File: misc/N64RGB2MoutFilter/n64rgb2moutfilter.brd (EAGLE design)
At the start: 107.6 x 29.5 mm, 35 parts

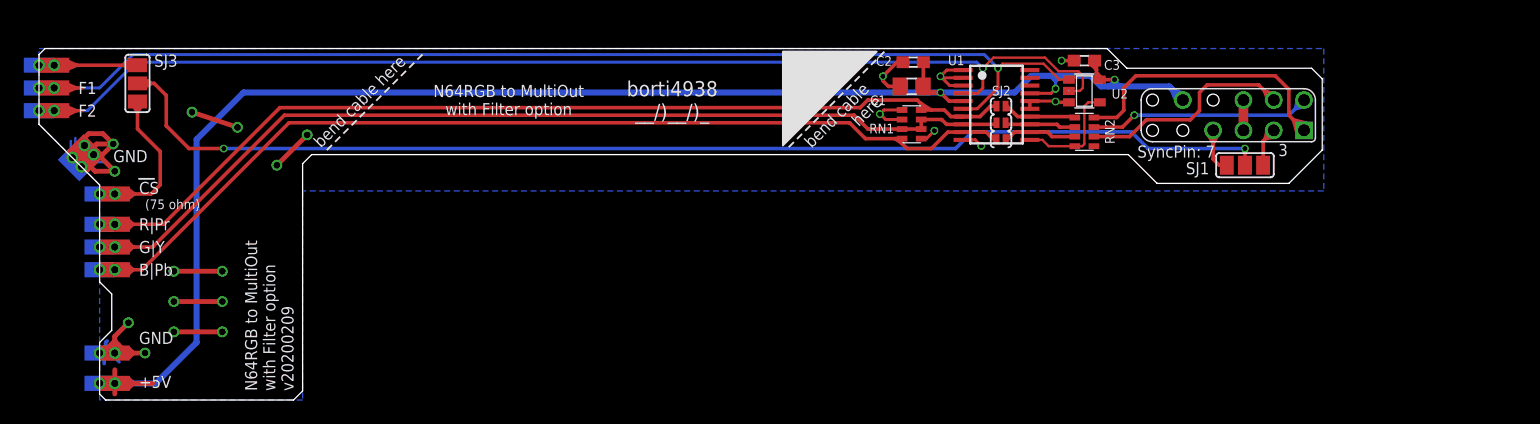
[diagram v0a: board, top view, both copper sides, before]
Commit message: adapt cable to fit with N64RGBv2.1
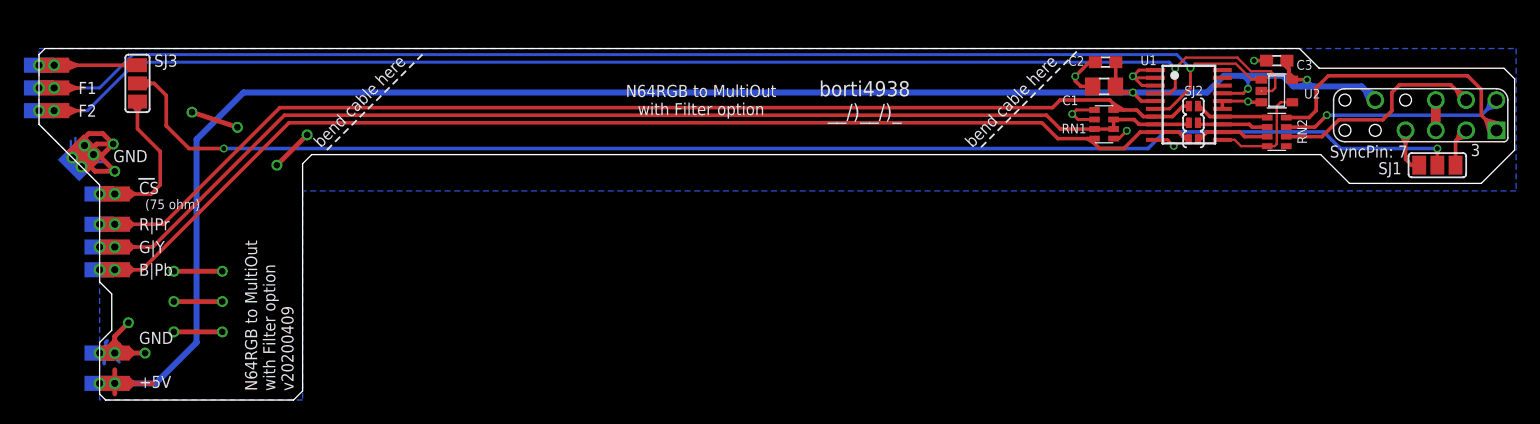
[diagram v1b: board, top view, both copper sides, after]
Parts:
- moved C1 16.1 mm to (89.3, 26.4)
- moved C2 16.1 mm to (89.4, 28.4)
- moved C3 16.1 mm to (103.8, 28.6)
- moved E$1 16.1 mm to (115.8, 24.0)
- moved RN1 16.1 mm to (89.3, 23.2)
- moved RN2 16.1 mm to (103.8, 22.6)
- moved SJ1 16.1 mm to (117.2, 19.8)
- moved SJ2B 16.1 mm to (96.8, 24.8)
- moved SJ2G 16.1 mm to (96.8, 23.4)
- moved SJ2R 16.1 mm to (96.8, 22.0)
- moved U1 16.1 mm to (96.4, 24.9)
- moved U2 16.1 mm to (103.8, 26.0)
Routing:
- net RED: track 86.1 -> 102.2 mm
- net F2: track 101.6 -> 117.7 mm
- net #CS.SEL: track 100.6 -> 116.8 mm
- net GREEN: track 84.9 -> 101.0 mm
- net F1: track 98.8 -> 114.9 mm
- net BLUE: track 87.5 -> 103.6 mm
- net 5V: track 139.2 -> 155.4 mm
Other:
- board size 107.6 x 29.5 mm -> 123.7 x 29.5 mm
- board text added: "N64RGB to MultiOut with Filter option v20200409"
- board text removed: "N64RGB to MultiOut with Filter option v20200209"
